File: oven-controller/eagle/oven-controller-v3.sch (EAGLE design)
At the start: 43 parts, among them Q1 FDV305N, Q2 FDV305N, Q3 FDV305N, Q4 FDV305N, U1 ARDUINO_SHIELDLONGPADS, U2 MAX31855, U3 MAX31855, U4 MAX31855, U5 MAX31855, U6 MAX31855

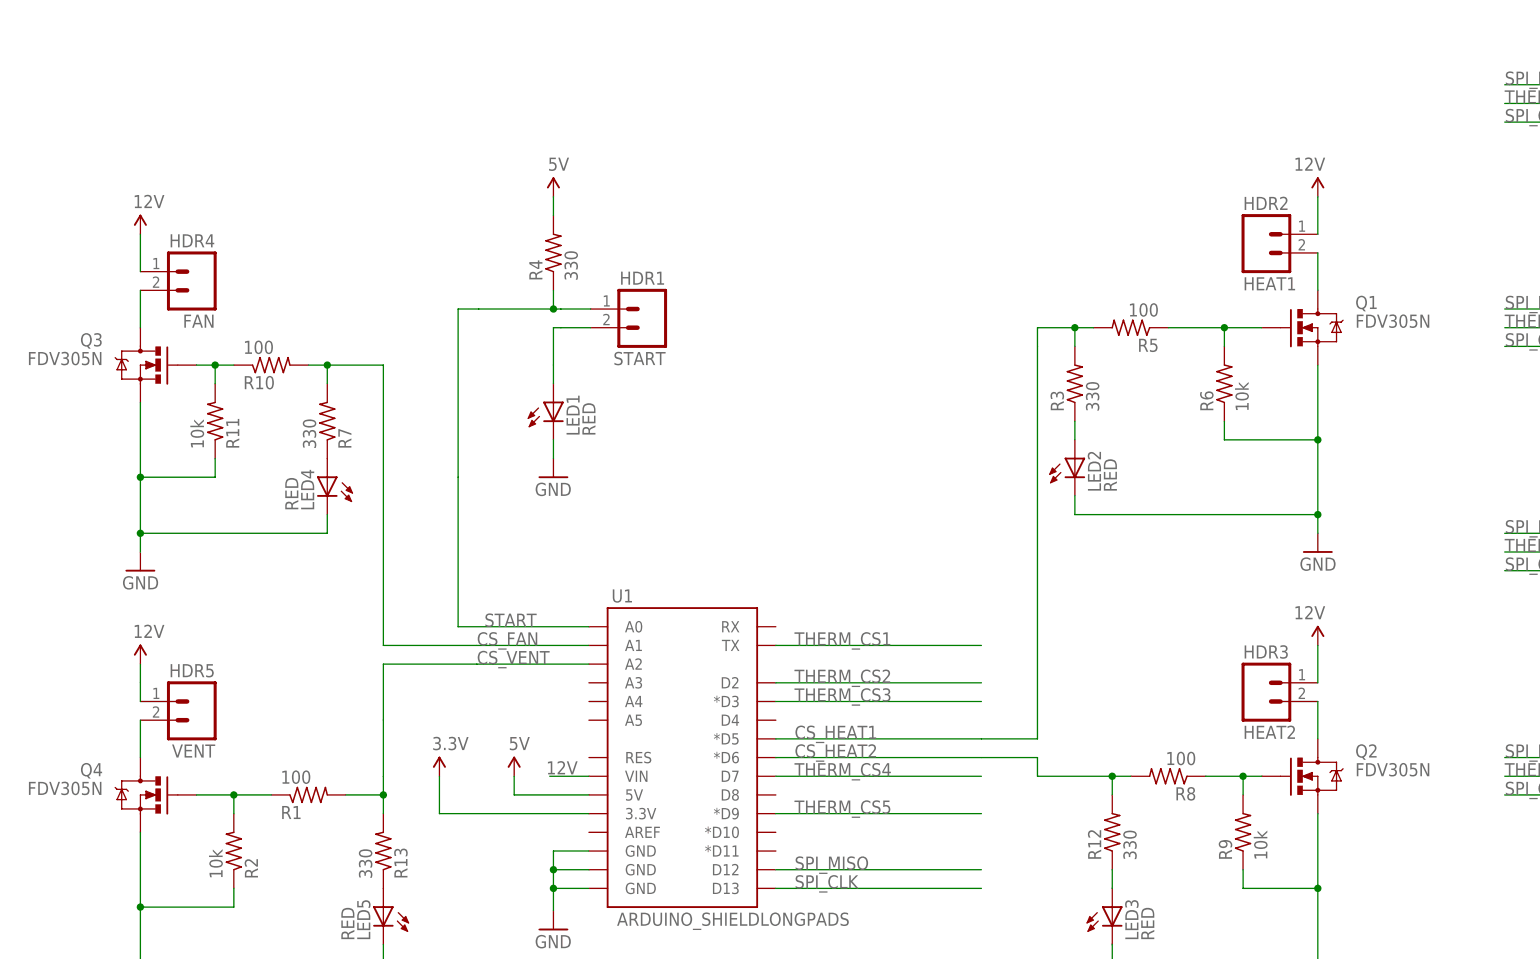
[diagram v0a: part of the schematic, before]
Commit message: Put diodes back in. Still need bypass caps.
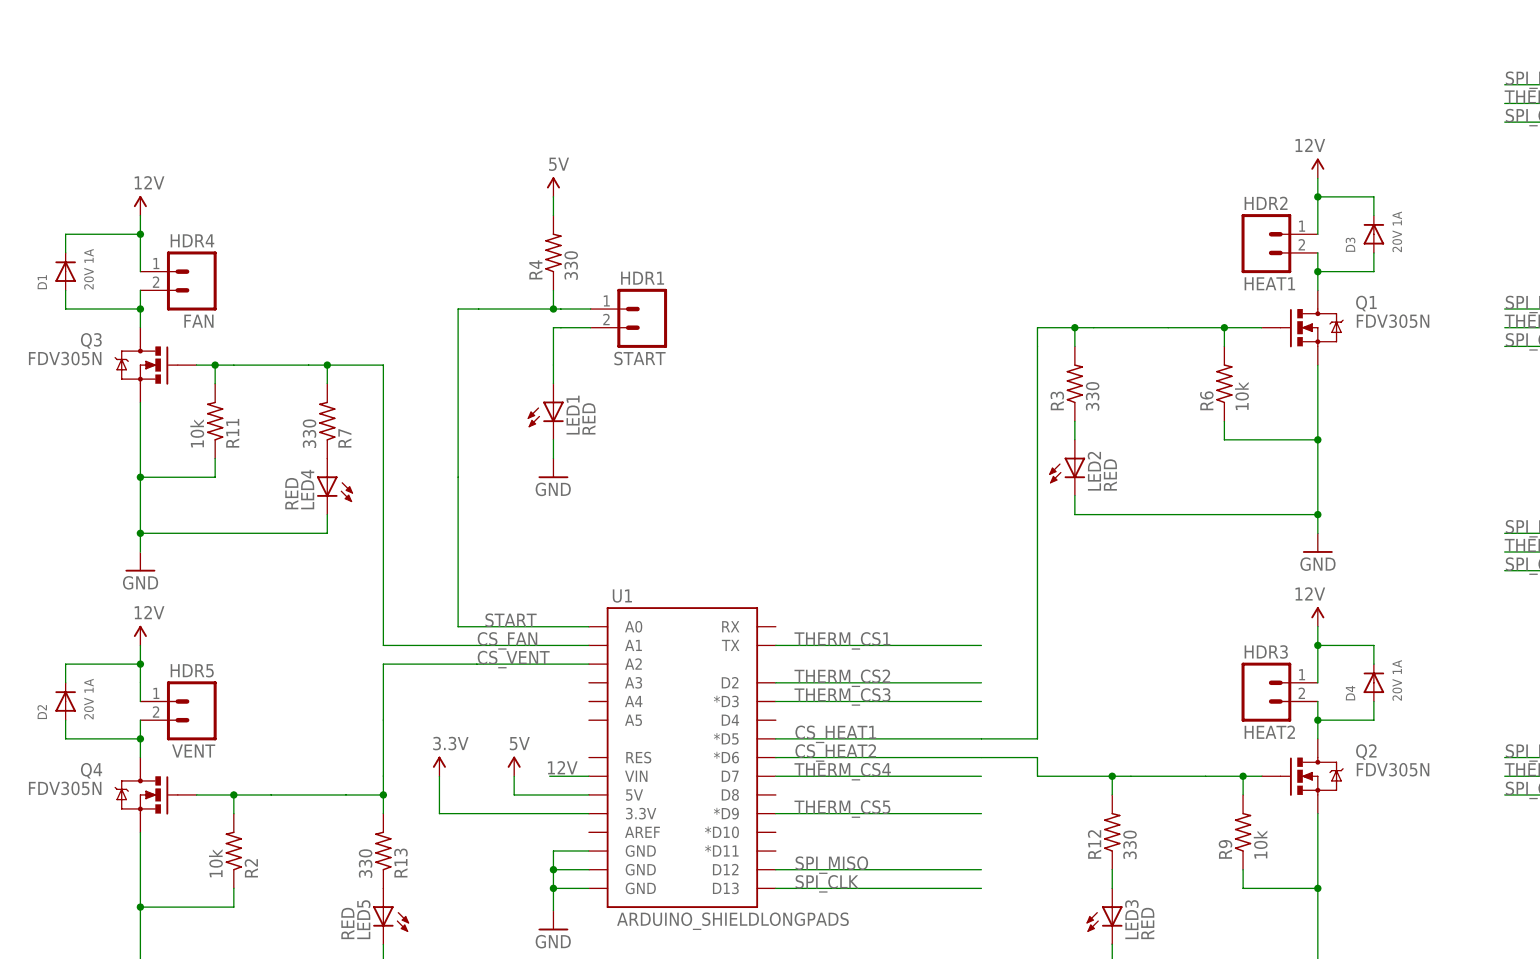
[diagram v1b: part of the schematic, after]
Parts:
- removed R1, R10, R5, R8: 100, rcl_custom:R-US_0603-C-NOSILK
- added D1, D2, D3, D4: 20V 1A, adafruit:DIODESMA
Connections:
- removed net N$1: Q1.G, R5.1, R6.2
- removed net N$2: Q4.G, R1.1, R2.2
- removed net N$20: Q2.G, R8.1, R9.2
- removed net N$22: Q3.G, R10.1, R11.2
- net 12V: now also D1.C, D2.C, D3.C, D4.C
- net CS_FAN: now also Q3.G, R11.2; no longer R10.2
- net CS_HEAT1: now also Q1.G, R6.2; no longer R5.2
- net CS_HEAT2: now also Q2.G, R9.2; no longer R8.2
- net CS_VENT: now also Q4.G, R2.2; no longer R1.2
- net HDR3: now also D1.A
- net N$21: now also D4.A
- net N$3: now also D2.A
- net N$4: now also D3.A

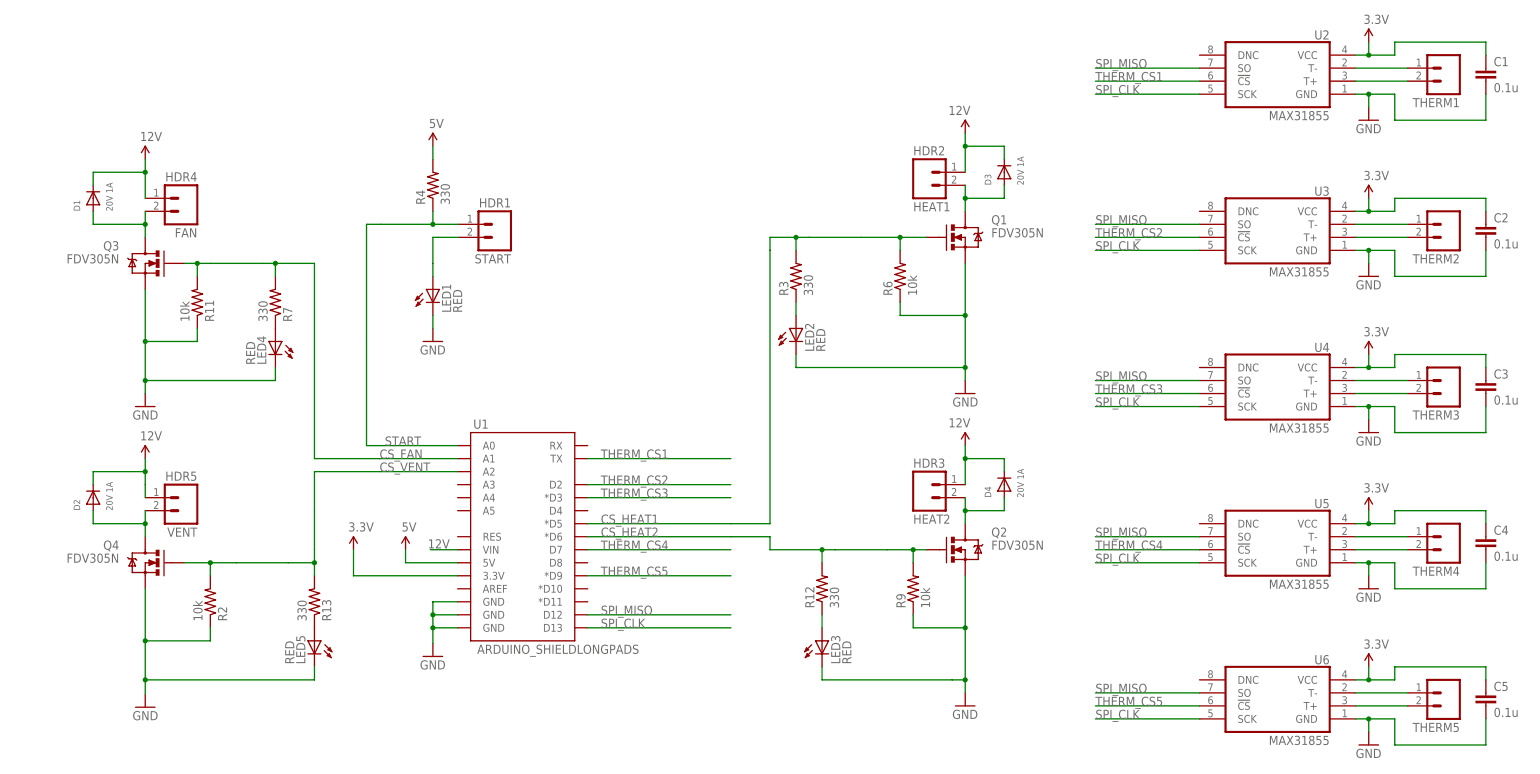
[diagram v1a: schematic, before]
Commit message: Added bypass caps. Ready for review.
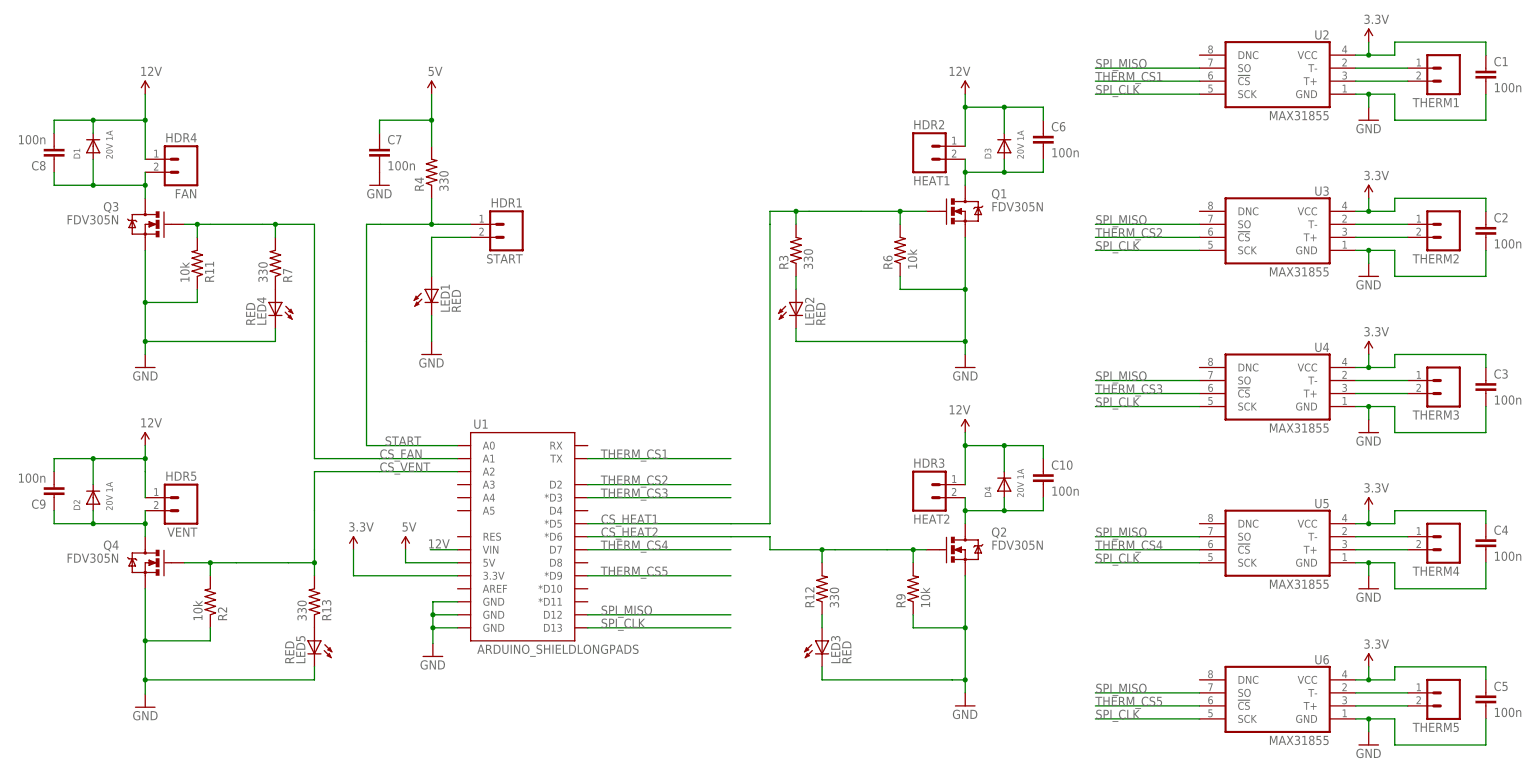
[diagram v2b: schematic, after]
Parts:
- added C10, C6, C7, C8, C9: 100n, rcl_custom:C-EUC0603K
- C1, C2, C3, C4, C5: value 0.1u -> 100n
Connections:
- net 12V: now also C10.1, C6.1, C8.2, C9.2
- net 5V: now also C7.1
- net GND: now also C7.2
- net HDR3: now also C8.1
- net N$21: now also C10.2
- net N$3: now also C9.1
- net N$4: now also C6.2
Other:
- moved on the sheet: D1, D3, FAN, HEAT1, LED2, LED4, Q1, Q3, R11, R3, R4, R6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

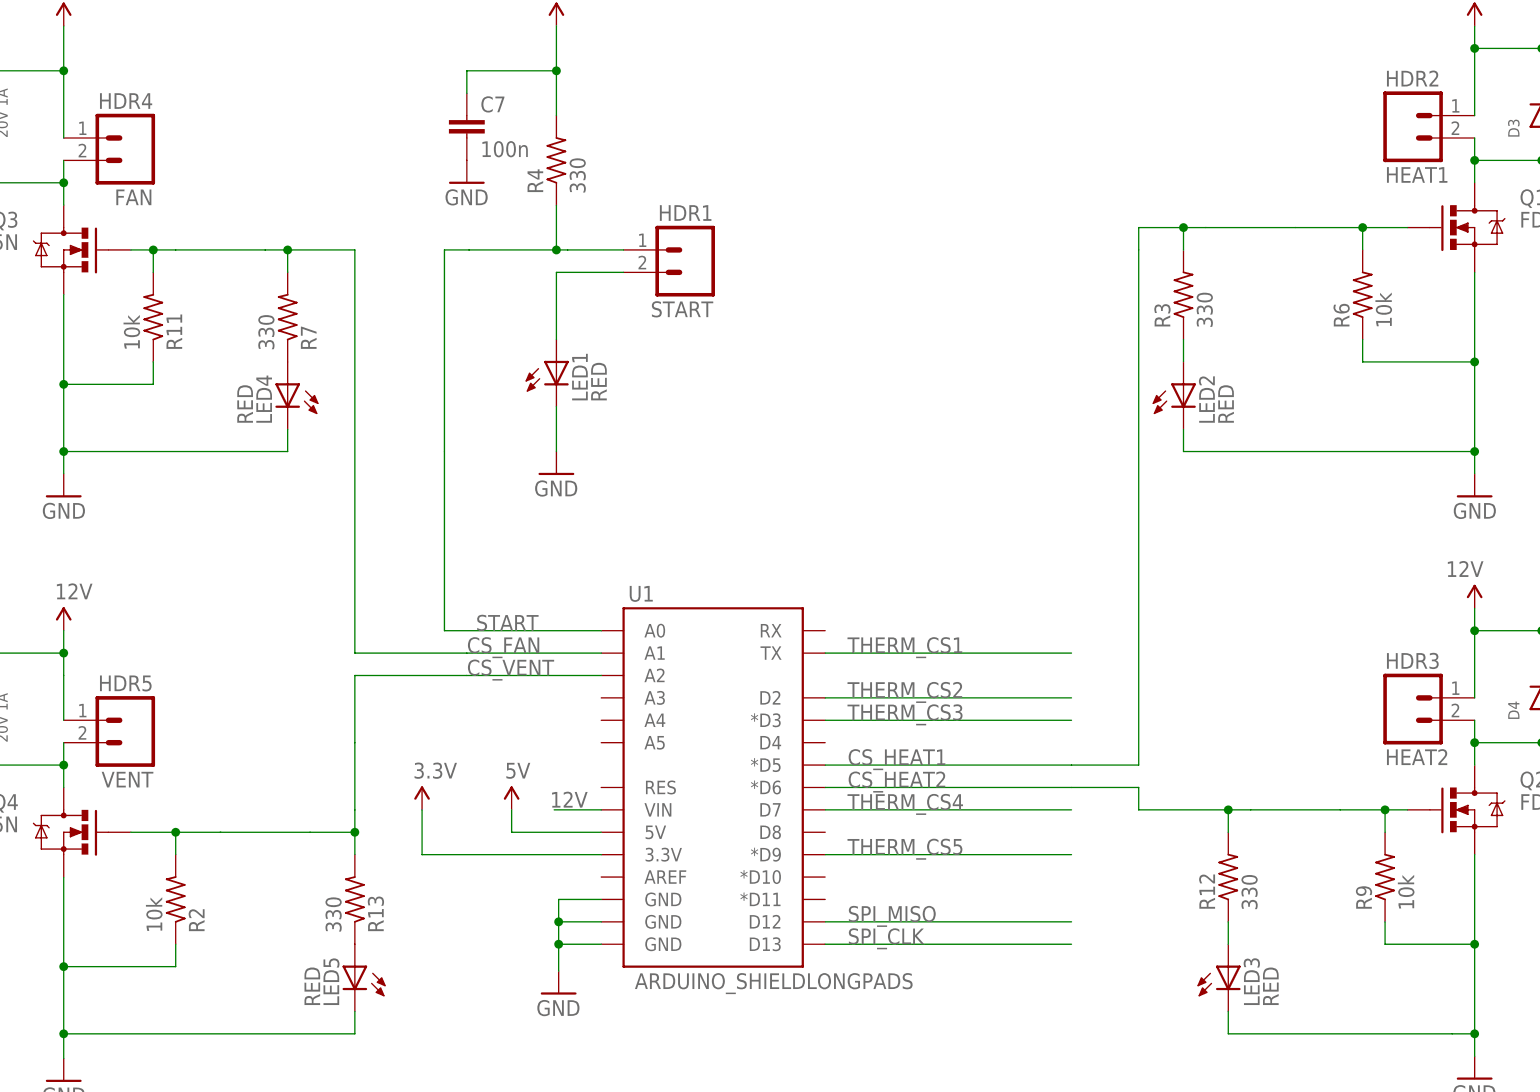
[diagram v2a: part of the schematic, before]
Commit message: Added BOM.
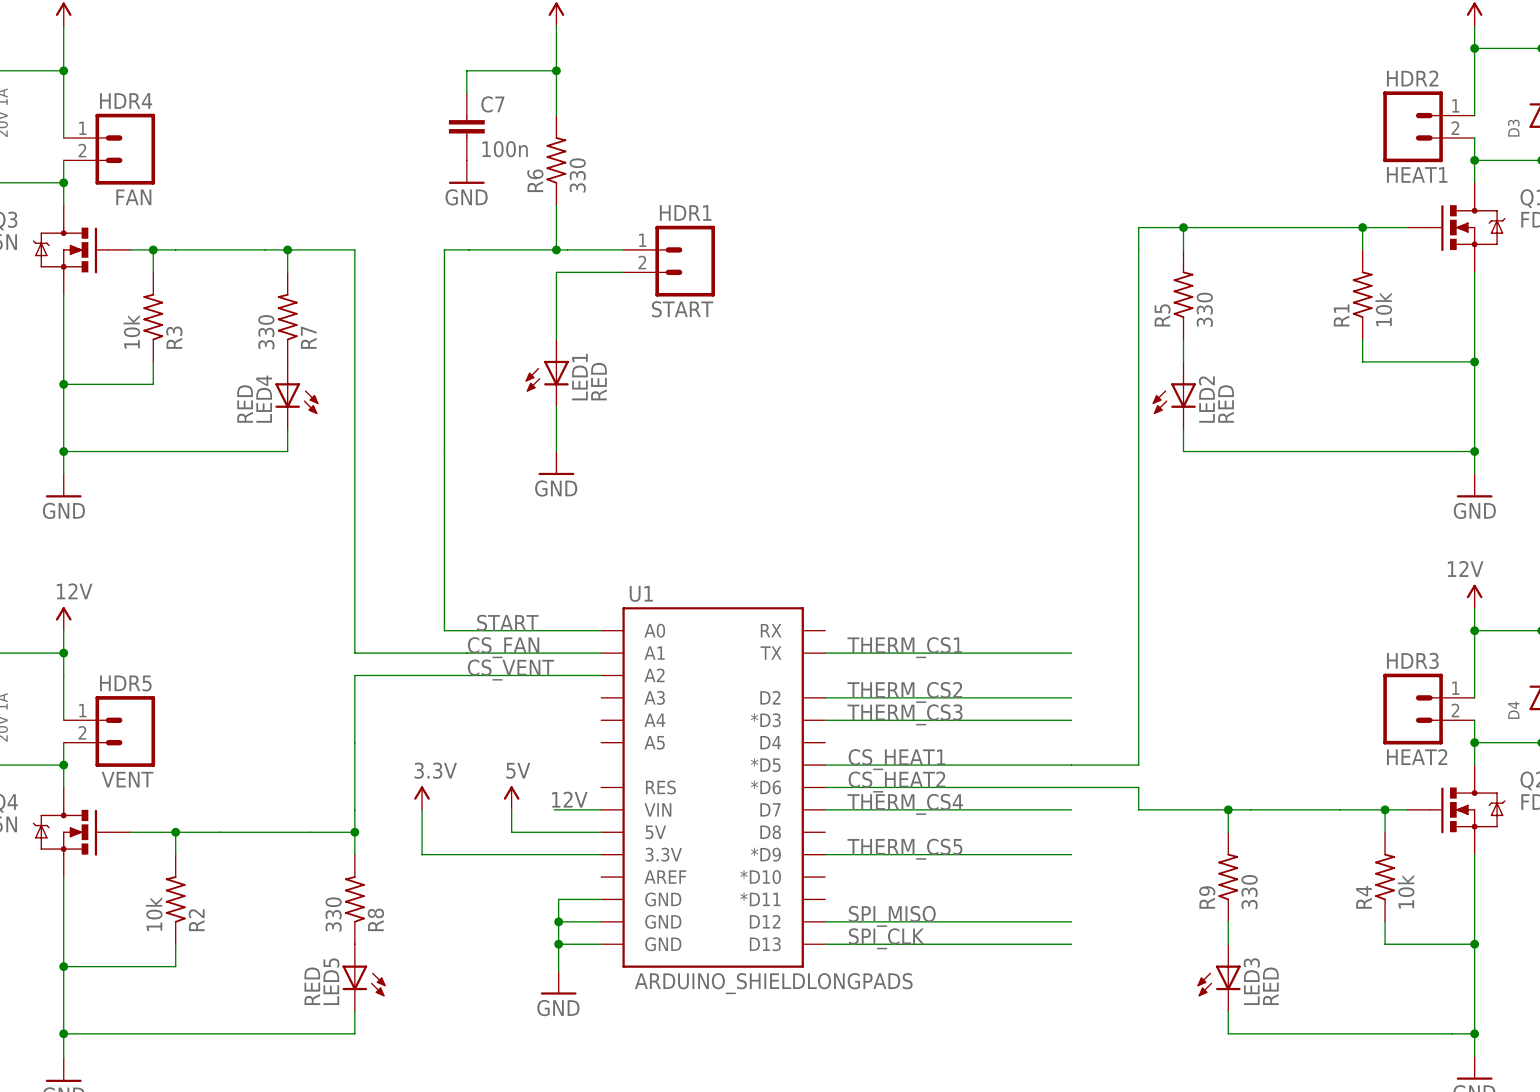
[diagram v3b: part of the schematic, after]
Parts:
- removed R11: 10k, rcl_custom:R-US_0603-C-NOSILK
- removed R12: 330, rcl_custom:R-US_0603-C-NOSILK
- added R1: 10k, rcl_custom:R-US_0603-C-NOSILK
- added R5: 330, rcl_custom:R-US_0603-C-NOSILK
- R3, R4: value 330 -> 10k
- R6, R9: value 10k -> 330
- renumbered R13 to R8
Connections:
- net 5V: now also R6.2; no longer R4.2
- net CS_FAN: now also R3.2; no longer R11.2
- net CS_HEAT1: now also R1.2, R5.2; no longer R3.2, R6.2
- net CS_HEAT2: now also R4.2; no longer R12.2
- net GND: now also R1.1, R3.1, R4.1; no longer R11.1, R6.1, R9.1
- net N$18: now also R9.1; no longer R12.1
- net N$7: now also R5.1; no longer R3.1
- net START: now also R6.1; no longer R4.1
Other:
- moved on the sheet: R3, R4, R6, R9

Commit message: Fixed diode package.
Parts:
- D1, D2, D3, D4: device adafruit:DIODESMA -> wicker:DIODE-DO214AC-SMA
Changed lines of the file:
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@@
 <part name="LED5" library="SparkFun-LED" deviceset="LED" device="0603" value="RED"/>
 <part name="R8" library="rcl_custom" deviceset="R-US_" device="0603-C-NOSILK" value="330"/>
-<part name="D1" library="adafruit" deviceset="DIODE" device="SMA" value="20V 1A"/>
-<part name="D2" library="adafruit" deviceset="DIODE" device="SMA" value="20V 1A"/>
-<part name="D3" library="adafruit" deviceset="DIODE" device="SMA" value="20V 1A"/>
-<part name="D4" library="adafruit" deviceset="DIODE" device="SMA" value="20V 1A"/>
+<part name="D1" library="wicker" deviceset="DIODE-DO214AC-SMA" device="" value="20V 1A"/>
+<part name="D2" library="wicker" deviceset="DIODE-DO214AC-SMA" device="" value="20V 1A"/>
+<part name="D3" library="wicker" deviceset="DIODE-DO214AC-SMA" device="" value="20V 1A"/>
+<part name="D4" library="wicker" deviceset="DIODE-DO214AC-SMA" device="" value="20V 1A"/>
 <part name="C6" library="rcl_custom" deviceset="C-EU" device="C0603K" value="100n"/>
 <part name="C7" library="rcl_custom" deviceset="C-EU" device="C0603K" value="100n"/>
